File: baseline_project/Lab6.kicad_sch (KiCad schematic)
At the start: 5 parts, among them IC1 TM4C123GH6PMIR, SW101 UP, U1 Adafruit ST7735R

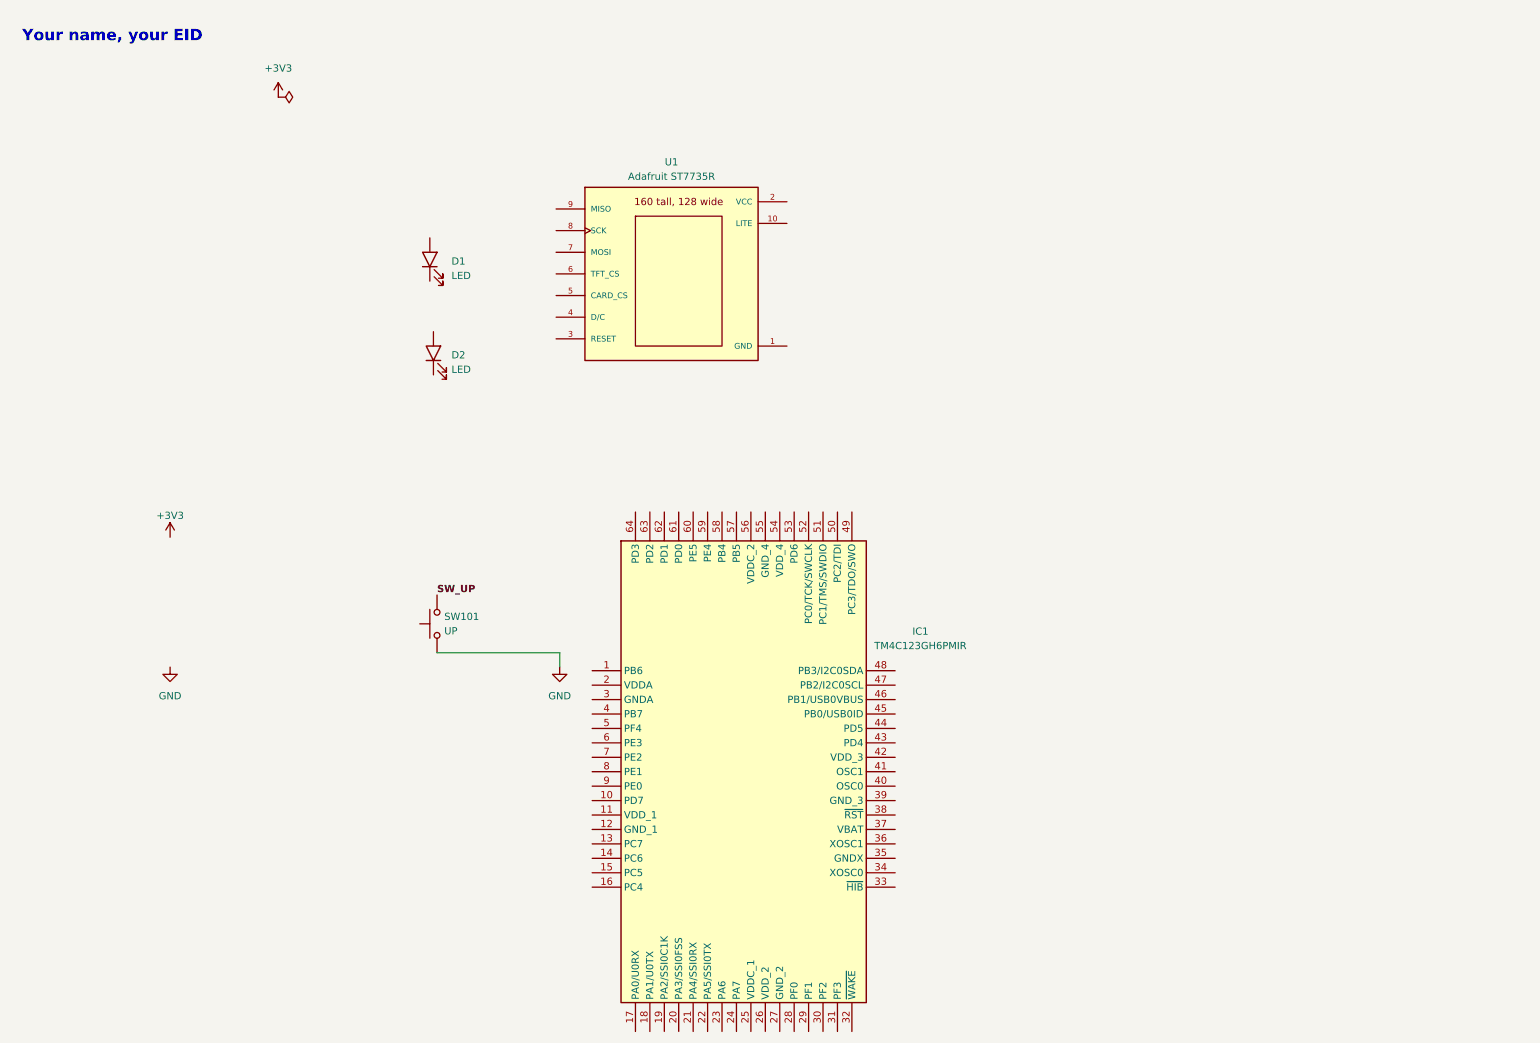
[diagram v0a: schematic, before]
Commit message: Lab6 starter version 2
Needs some starter PCB place and trace
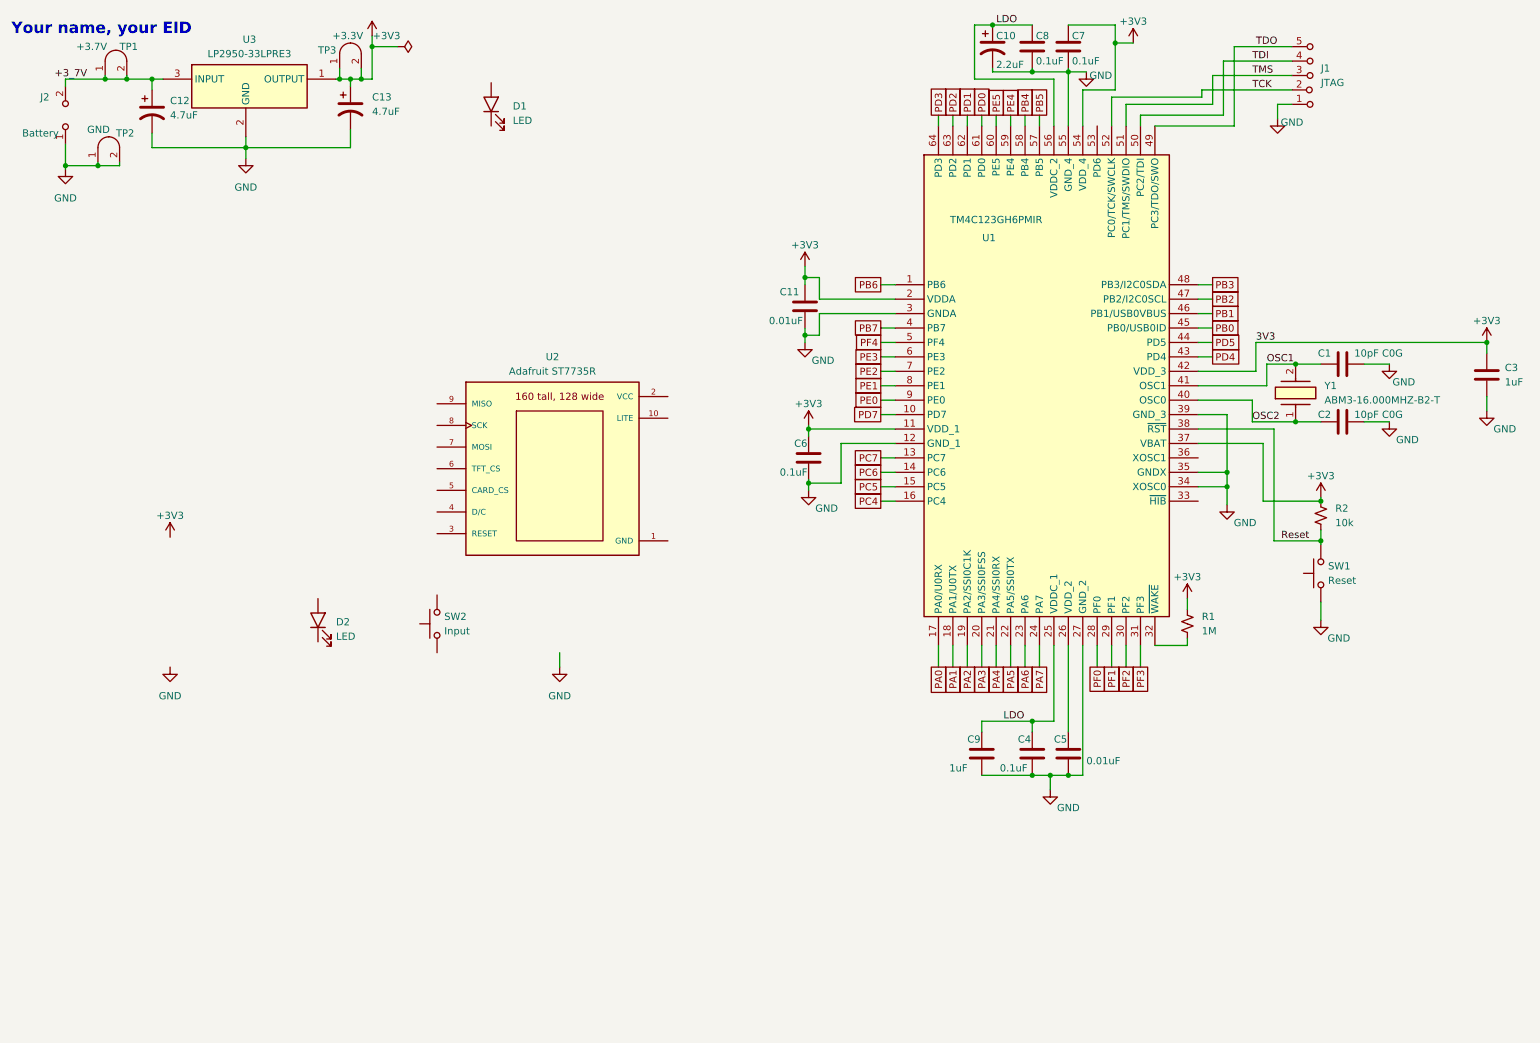
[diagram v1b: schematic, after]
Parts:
- added C1, C2: 10pF C0G, ECE445L:C_Axial_200mil, symbol ECE445L:C
- added C10: 2.2uF, ECE445L:CP_Radial_Tantal200mil, symbol ECE445L:C_Polarized
- added C11, C5: 0.01uF, ECE445L:C_Axial_200mil, symbol ECE445L:C
- added C12, C13: 4.7uF, ECE445L:CP_Radial_Tantal200mil, symbol ECE445L:C_Polarized
- added C3, C9: 1uF, ECE445L:C_Axial_200mil, symbol ECE445L:C
- added C4, C6, C7, C8: 0.1uF, ECE445L:C_Axial_200mil, symbol ECE445L:C
- added J1: JTAG, ECE445L:PinHeader_1x05_P2.54mm_Vertical, symbol ECE445L:Header_5
- added J2: Battery, ECE445L:PinHeader_1x02_P2.54mm_Vertical, symbol ECE445L:Header_2
- added R1: 1M, ECE445L:R_Axial_DIN0204_L3.6mm_D1.6mm_P7.62mm_Horizontal, symbol ECE445L:R_0.125W
- added R2: 10k, ECE445L:R_Axial_DIN0204_L3.6mm_D1.6mm_P7.62mm_Horizontal, symbol ECE445L:R_0.125W
- added SW1: Reset, Button_Switch_THT:SW_PUSH_6mm, symbol Switch:SW_Push
- added TP1: +3.7V, ECE445L:Testpoint_1x02_P2.54mm, symbol ECE445L:Testpoint
- added TP2: GND, ECE445L:Testpoint_1x02_P2.54mm, symbol ECE445L:Testpoint
- added TP3: +3.3V, ECE445L:Testpoint_1x02_P2.54mm, symbol ECE445L:Testpoint
- added U3: LP2950-33LPRE3, ECE445L:TL431CLPM, symbol LP2950-33LPRE3:LP2950-33LPRE3
- added Y1: ABM3-16.000MHZ-B2-T, ECE445L:ABM3, symbol ABM3-16_000MHZ-B2-T:ABM3-16.000MHZ-B2-T
- SW2: renamed from SW101; value UP -> Input
- renumbered IC1 to U1, U1 to U2
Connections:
- net +3V3: now also U1.11 (VDD_1), U1.2 (VDDA), U1.37 (VBAT), U1.42 (VDD_3), U1.54 (VDD_4), C11.1, C13.1, C3.1, C6.1, C7.1, R1.1, R2.1, TP3.1 (A), TP3.2 (B), U3.1 (OUTPUT)
- net GND: now also U1.12 (GND_1), U1.27 (GND_2), U1.3 (GNDA), U1.34 (XOSC0), U1.35 (GNDX), U1.39 (GND_3), U1.55 (GND_4), C1.2, C10.2, C11.2, C12.2, C13.2, C2.2, C3.2, C4.2, C5.2, C6.2, C7.2, C8.2, C9.2, J1.1 (A), J2.1 (A), SW1.1, TP2.1 (A), TP2.2 (B), U3.2 (GND); no longer SW2.1
- net PB6: now reaches U1.1 (PB6)
- net PD7: now reaches U1.10 (PD7)
- net PC7: now reaches U1.13 (PC7)
- net PC6: now reaches U1.14 (PC6)
- net PC5: now reaches U1.15 (PC5)
- net PC4: now reaches U1.16 (PC4)
- net PA0: now reaches U1.17 (PA0/U0RX)
- net PA1: now reaches U1.18 (PA1/U0TX)
- net PA2: now reaches U1.19 (PA2/SSI0C1K)
- net PA3: now reaches U1.20 (PA3/SSI0FSS)
- net PA4: now reaches U1.21 (PA4/SSI0RX)
- net PA5: now reaches U1.22 (PA5/SSI0TX)
- net PA6: now reaches U1.23 (PA6)
- net PA7: now reaches U1.24 (PA7)
- net LDO: now reaches U1.25 (VDDC_1)
- net LDO: now also U1.56 (VDDC_2), C10.1, C4.1, C8.1, C9.1
- net at U1.26 (VDD_2): now also C5.1
- net PF0: now reaches U1.28 (PF0)
- net PF1: now reaches U1.29 (PF1)
- net PF2: now reaches U1.30 (PF2)
- net PF3: now reaches U1.31 (PF3)
- net at U1.32 (~{WAKE}): now also R1.2
- net Reset: now reaches U1.38 (~{RST})
- net Reset: now also R2.2, SW1.2
- net PB7: now reaches U1.4 (PB7)
- net OSC2: now reaches U1.40 (OSC0)
- net OSC2: now also C2.1, Y1.1
- net OSC1: now reaches U1.41 (OSC1)
- net OSC1: now also C1.1, Y1.2
- net PD4: now reaches U1.43 (PD4)
- net PD5: now reaches U1.44 (PD5)
- net PB0: now reaches U1.45 (PB0/USB0ID)
- net PB1: now reaches U1.46 (PB1/USB0VBUS)
- net PB2: now reaches U1.47 (PB2/I2C0SCL)
- net PB3: now reaches U1.48 (PB3/I2C0SDA)
- net TDO: now reaches U1.49 (PC3/TDO/SWO)
- net TDO: now also J1.5 (C)
- net PF4: now reaches U1.5 (PF4)
- net TDI: now reaches U1.50 (PC2/TDI)
- net TDI: now also J1.4 (C)
- net TMS: now reaches U1.51 (PC1/TMS/SWDIO)
- net TMS: now also J1.3 (C)
- net TCK: now reaches U1.52 (PC0/TCK/SWCLK)
- net TCK: now also J1.2 (B)
- net PB5: now reaches U1.57 (PB5)
- net PB4: now reaches U1.58 (PB4)
- net PE4: now reaches U1.59 (PE4)
- net PE3: now reaches U1.6 (PE3)
- net PE5: now reaches U1.60 (PE5)
- net PD0: now reaches U1.61 (PD0)
- net PD1: now reaches U1.62 (PD1)
- net PD2: now reaches U1.63 (PD2)
- net PD3: now reaches U1.64 (PD3)
- net PE2: now reaches U1.7 (PE2)
- net PE1: now reaches U1.8 (PE1)
- net PE0: now reaches U1.9 (PE0)
- net SW_UP: no longer names the net of SW2.2
- new net +3_7V: C12.1, J2.2 (B), TP1.1 (A), TP1.2 (B), U3.3 (INPUT)
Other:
- moved on the sheet: D1, D2, U1, U2

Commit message: Lab6 starter
I am ready to release Lab6 starter and updated ECE445L library
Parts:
- added H1, H2, H3, H4: ~, ECE445L:MountingHole_4_40, symbol ECE445L:MountingHole
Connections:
- net +3V3: now also C5.1, U1.26 (VDD_2)
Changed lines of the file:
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@@
   (junction (at 71.755 23.495) (diameter 0) (color 0 0 0 0)
   )
+  (junction (at 200.025 137.795) (diameter 0) (color 0 0 0 0)
+  )
   (junction (at 227.965 95.25) (diameter 0) (color 0 0 0 0)
   )
@@
     (stroke (width 0) (type default))
   )
-  (wire (pts (xy 200.025 123.19) (xy 200.025 138.43))
+  (wire (pts (xy 200.025 123.19) (xy 200.025 137.795))
     (stroke (width 0) (type default))
   )
@@
     (stroke (width 0) (type default))
   )
+  (wire (pts (xy 200.025 137.795) (xy 200.025 138.43))
+    (stroke (width 0) (type default))
+  )
   (wire (pts (xy 30.48 22.86) (xy 30.48 23.495))
     (stroke (width 0) (type default))
@@
   )
   (wire (pts (xy 38.735 23.495) (xy 38.735 25.4))
+    (stroke (width 0) (type default))
+  )
+  (wire (pts (xy 200.025 137.795) (xy 206.375 137.795))
     (stroke (width 0) (type default))
   )
@@
     )
   )
+  (symbol (lib_id "power:+3V3") (at 206.375 137.795 0) (unit 1)
+    (in_bom yes) (on_board yes) (dnp no)
+    (property "Reference" "#PWR010" (at 206.375 141.605 0)
+      (effects (font (size 1.27 1.27)) hide)
+    )
+    (property "Value" "+3V3" (at 206.375 133.985 0)
+      (effects (font (size 1.27 1.27)))
+    )
+    (property "Footprint" "" (at 206.375 137.795 0)
+      (effects (font (size 1.27 1.27)) hide)
+    )
+    (property "Datasheet" "" (at 206.375 137.795 0)
+      (effects (font (size 1.27 1.27)) hide)
+    )
+    (pin "1")
+    (instances
+      (project "Lab6"
+        (path "/69b823fd-c065-40ff-9bb9-c5835555f3eb"
+          (reference "#PWR010") (unit 1)
+        )
+      )
+    )
+  )
   (symbol (lib_id "ECE445L:C") (at 193.675 142.24 0) (unit 1)
     (in_bom yes) (on_board yes) (dnp no)
@@
         (path "/69b823fd-c065-40ff-9bb9-c5835555f3eb"
           (reference "C4") (unit 1)
+        )
+      )
+    )
+  )
+  (symbol (lib_id "ECE445L:MountingHole") (at 276.225 28.575 0) (unit 1)
+    (in_bom yes) (on_board yes) (dnp no) (fields_autoplaced)
+    (property "Reference" "H3" (at 272.415 26.67 0)
+      (effects (font (size 1.27 1.27)))
+    )
+    (property "Value" "~" (at 276.225 28.575 0)
+      (effects (font (size 1.27 1.27)))
+    )
+    (property "Footprint" "ECE445L:MountingHole_4_40" (at 276.225 28.575 0)
+      (effects (font (size 1.27 1.27)) hide)
+    )
+    (property "Datasheet" "" (at 276.225 28.575 0)
+      (effects (font (size 1.27 1.27)) hide)
+    )
+    (pin "1")
+    (instances
+      (project "Lab6"
+        (path "/69b823fd-c065-40ff-9bb9-c5835555f3eb"
+          (reference "H3") (unit 1)
         )
       )
@@
     )
   )
+  (symbol (lib_id "ECE445L:MountingHole") (at 276.225 18.415 0) (unit 1)
+    (in_bom yes) (on_board yes) (dnp no) (fields_autoplaced)
+    (property "Reference" "H1" (at 272.415 16.51 0)
+      (effects (font (size 1.27 1.27)))
+    )
+    (property "Value" "~" (at 276.225 18.415 0)
+      (effects (font (size 1.27 1.27)))
+    )
+    (property "Footprint" "ECE445L:MountingHole_4_40" (at 276.225 18.415 0)
+      (effects (font (size 1.27 1.27)) hide)
+    )
+    (property "Datasheet" "" (at 276.225 18.415 0)
+      (effects (font (size 1.27 1.27)) hide)
+    )
+    (pin "1")
+    (instances
+      (project "Lab6"
+        (path "/69b823fd-c065-40ff-9bb9-c5835555f3eb"
+          (reference "H1") (unit 1)
+        )
+      )
+    )
+  )
+  (symbol (lib_id "ECE445L:MountingHole") (at 276.225 23.495 0) (unit 1)
+    (in_bom yes) (on_board yes) (dnp no) (fields_autoplaced)
+    (property "Reference" "H2" (at 272.415 21.59 0)
+      (effects (font (size 1.27 1.27)))
+    )
+    (property "Value" "~" (at 276.225 23.495 0)
+      (effects (font (size 1.27 1.27)))
+    )
+    (property "Footprint" "ECE445L:MountingHole_4_40" (at 276.225 23.495 0)
+      (effects (font (size 1.27 1.27)) hide)
+    )
+    (property "Datasheet" "" (at 276.225 23.495 0)
+      (effects (font (size 1.27 1.27)) hide)
+    )
+    (pin "1")
+    (instances
+      (project "Lab6"
+        (path "/69b823fd-c065-40ff-9bb9-c5835555f3eb"
+          (reference "H2") (unit 1)
+        )
+      )
+    )
+  )
   (symbol (lib_id "power:+3V3") (at 273.685 69.85 0) (unit 1)
     (in_bom yes) (on_board yes) (dnp no)
@@
     )
   )
-  (symbol (lib_id "power:GND") (at 41.91 127 0) (unit 1)
+  (symbol (lib_id "power:GND") (at 58.42 84.455 0) (unit 1)
     (in_bom yes) (on_board yes) (dnp no) (fields_autoplaced)
-    (property "Reference" "#PWR0102" (at 41.91 133.35 0)
-      (effects (font (size 1.27 1.27)) hide)
-    )
-    (property "Value" "GND" (at 41.91 132.08 0)
-      (effects (font (size 1.27 1.27)))
-    )
-    (property "Footprint" "" (at 41.91 127 0)
-      (effects (font (size 1.27 1.27)) hide)
-    )
-    (property "Datasheet" "" (at 41.91 127 0)
+    (property "Reference" "#PWR0102" (at 58.42 90.805 0)
+      (effects (font (size 1.27 1.27)) hide)
+    )
+    (property "Value" "GND" (at 58.42 89.535 0)
+      (effects (font (size 1.27 1.27)))
+    )
+    (property "Footprint" "" (at 58.42 84.455 0)
+      (effects (font (size 1.27 1.27)) hide)
+    )
+    (property "Datasheet" "" (at 58.42 84.455 0)
       (effects (font (size 1.27 1.27)) hide)
     )
@@
         )
       )
+    )
+  )
+  (symbol (lib_id "ECE445L:MountingHole") (at 276.225 33.655 0) (unit 1)
+    (in_bom yes) (on_board yes) (dnp no) (fields_autoplaced)
+    (property "Reference" "H4" (at 272.415 31.75 0)
+      (effects (font (size 1.27 1.27)))
+    )
+    (property "Value" "~" (at 276.225 33.655 0)
+      (effects (font (size 1.27 1.27)))
+    )
+    (property "Footprint" "ECE445L:MountingHole_4_40" (at 276.225 33.655 0)
+      (effects (font (size 1.27 1.27)) hide)
+    )
+    (property "Datasheet" "" (at 276.225 33.655 0)
+      (effects (font (size 1.27 1.27)) hide)
+    )
+    (pin "1")
+    (instances
+      (project "Lab6"
+        (path "/69b823fd-c065-40ff-9bb9-c5835555f3eb"
+          (reference "H4") (unit 1)
+        )
+      )

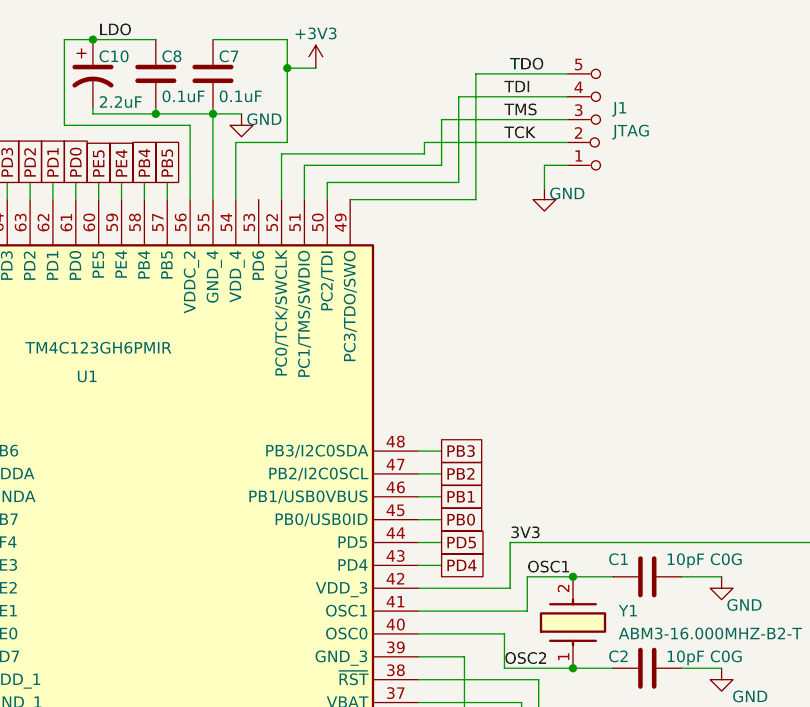
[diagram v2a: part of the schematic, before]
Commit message: added PD6
fixed ERC error with two +3V3 nets
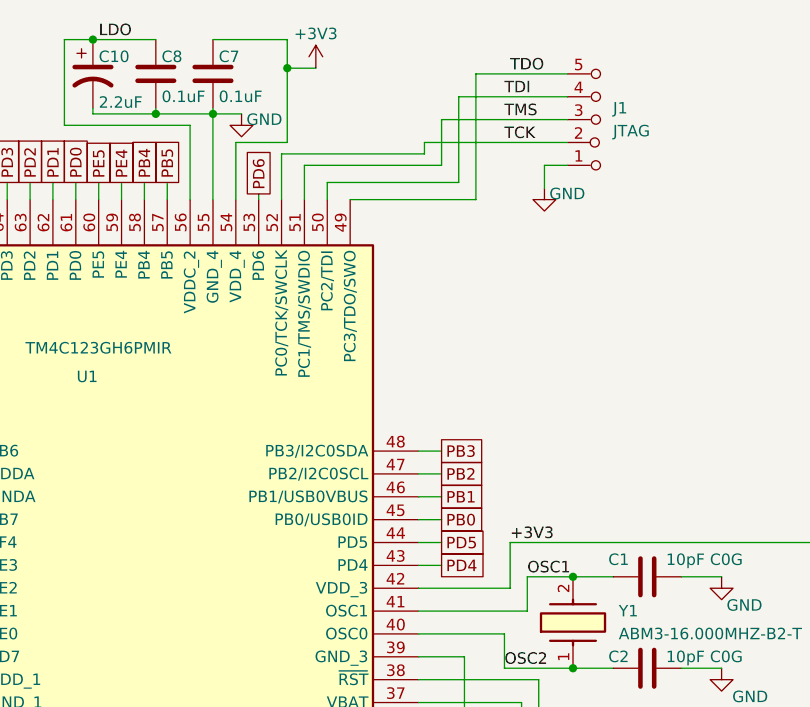
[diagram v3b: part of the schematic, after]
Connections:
- net PD6: now reaches U1.53 (PD6)
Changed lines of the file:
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@@
   (title_block
     (title "ECE 445L Lab6 Project")
-    (date "2024-02-20")
-    (rev "v1.0.0")
+    (date "2024-02-27")
+    (rev "v1.0.1")
     (company "The University of Texas at Austin")
   )
@@
   )
   (wire (pts (xy 167.005 95.25) (xy 169.545 95.25))
+    (stroke (width 0) (type default))
+  )
+  (wire (pts (xy 205.105 31.115) (xy 205.105 31.75))
     (stroke (width 0) (type default))
   )
@@
     (effects (font (size 1.27 1.27)) (justify left bottom))
   )
-  (label "3V3" (at 233.045 69.85 0) (fields_autoplaced)
+  (label "+3V3" (at 233.045 69.85 0) (fields_autoplaced)
     (effects (font (size 1.27 1.27)) (justify left bottom))
   )
@@
     )
   )
+  (global_label "PD6" (shape passive) (at 205.105 31.115 90) (fields_autoplaced)
+    (effects (font (size 1.27 1.27)) (justify left))
+    (property "Intersheetrefs" "${INTERSHEET_REFS}" (at 205.105 25.4916 90)
+      (effects (font (size 1.27 1.27)) (justify left) hide)
+    )
+  )
